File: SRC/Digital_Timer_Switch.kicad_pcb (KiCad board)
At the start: 2 copper layers, 82.5 x 76.2 mm, 65 parts, among them J101 AC_IN, J102 Conn_VIN, J103 AC_OUT, Q101 AO3401A, Q201 AO3401A, Q401 MMBT3904, SW301 SW_AUTO, SW302 SW_TIME, SW303 SW_DAY, SW304 SW_RST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

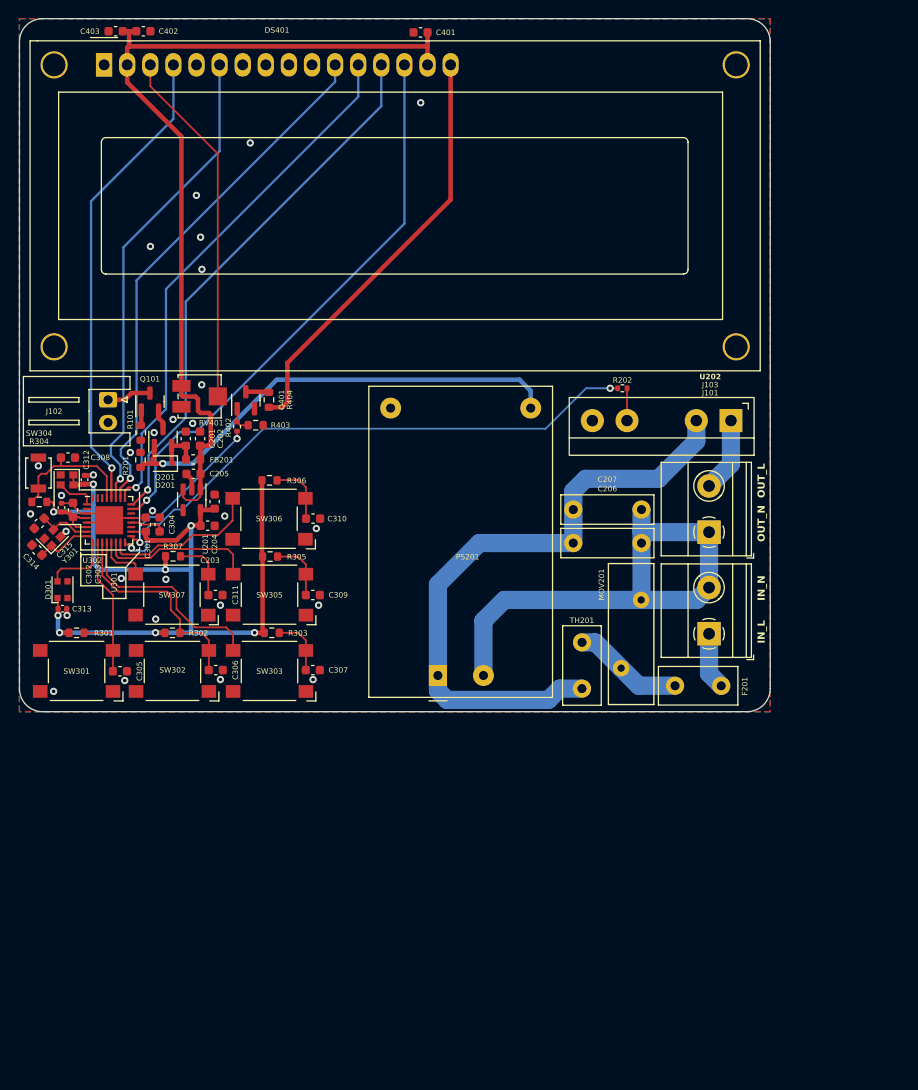
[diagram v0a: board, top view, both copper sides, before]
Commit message: Added debug testpoints.
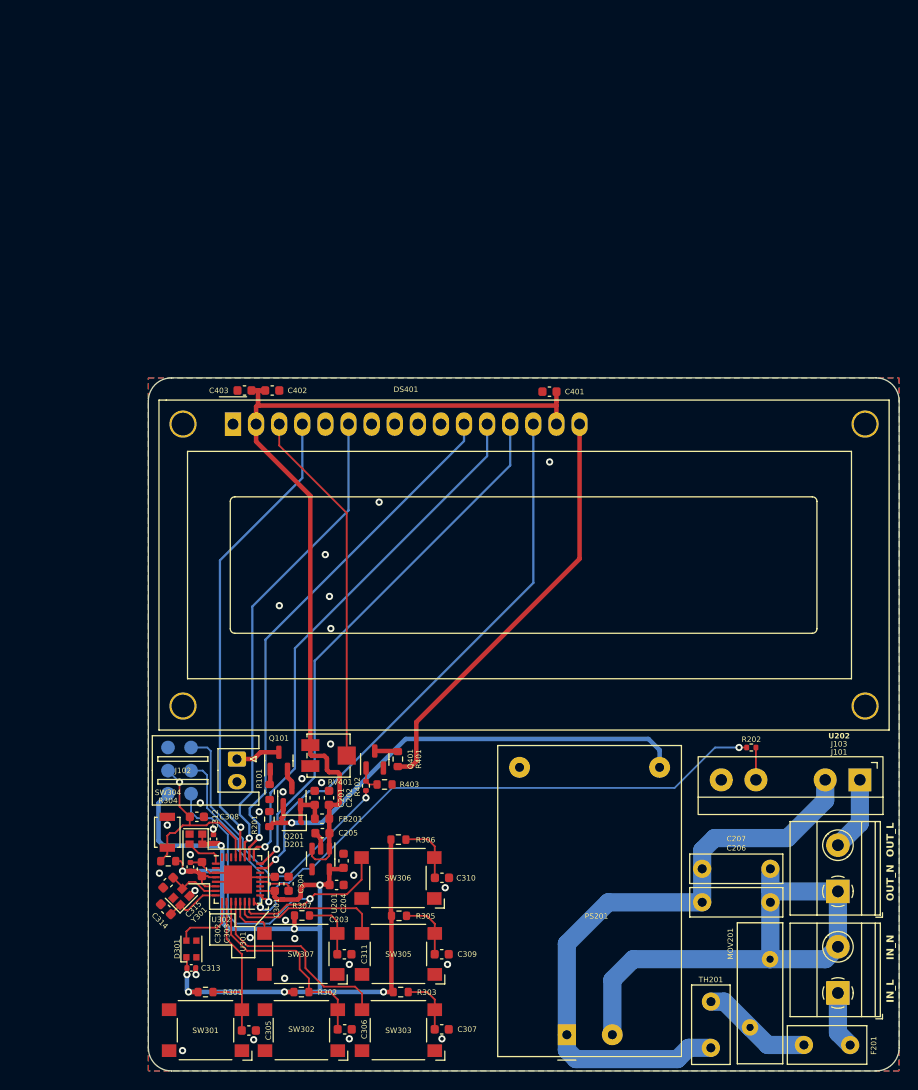
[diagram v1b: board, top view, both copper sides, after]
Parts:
- added TP301: TP_MOSI, TestPoint:TestPoint_Pad_D1.5mm, B.Cu at (107.8, 110.6)
- added TP302: TP_VCC, TestPoint:TestPoint_Pad_D1.5mm, B.Cu at (105.2, 110.6)
- added TP303: TP_MISO, TestPoint:TestPoint_Pad_D1.5mm, B.Cu at (107.8, 108.1)
- added TP304: TP_RST, TestPoint:TestPoint_Pad_D1.5mm, B.Cu at (105.2, 108.1)
- added TP305: TP_SCK, TestPoint:TestPoint_Pad_D1.5mm, B.Cu at (107.8, 105.5)
- added TP306: TP_GND, TestPoint:TestPoint_Pad_D1.5mm, B.Cu at (105.2, 105.5)
- moved MOV201 42.0 mm to (169.2, 136.3)
- moved R303 42.0 mm to (130.8, 132.4)
- moved C202 42.0 mm to (122.9, 111.1)
- moved C205 42.0 mm to (122.2, 115.0)
- moved C306 42.0 mm to (124.7, 136.5)
- moved C308 42.0 mm to (108.4, 113.2)
- moved C309 42.0 mm to (135.3, 128.3)
- moved C311 42.0 mm to (124.6, 128.3)
- moved C312 42.0 mm to (110.2, 115.6)
- moved C315 42.0 mm to (105.3, 120.4)
- moved C401 42.0 mm to (147.2, 66.4)
- moved D201 42.0 mm to (118.8, 113.8)
- moved FB201 42.0 mm to (122.2, 113.4)
- moved J103 42.0 mm to (178.9, 121.4)
- moved PS201 42.0 mm to (149.1, 137.1)
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- renumbered R404 to R401
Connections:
- net /Digital_Timer_Switch_Power/RELAY_EN renamed /MCU_ATMEGA328P-M/PB4
- net /MCU_ATMEGA328P-M/BTN_AUTO renamed /MCU_ATMEGA328P-M/PD6
- net /MCU_ATMEGA328P-M/BTN_DAY renamed /MCU_ATMEGA328P-M/PB0
- net /MCU_ATMEGA328P-M/BTN_HOUR renamed /MCU_ATMEGA328P-M/PB2
- net /MCU_ATMEGA328P-M/BTN_MIN renamed /MCU_ATMEGA328P-M/PB3
- net /MCU_ATMEGA328P-M/BTN_PROG renamed /MCU_ATMEGA328P-M/PB1
- net /MCU_ATMEGA328P-M/BTN_TIME renamed /MCU_ATMEGA328P-M/PD7
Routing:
- net /MCU_ATMEGA328P-M/PB3: track 24.5 -> 51.0 mm, vias 0 -> 1
- net /MCU_ATMEGA328P-M/PB5: track 18.5 -> 37.8 mm
- net /MCU_ATMEGA328P-M/PB4: track 63.2 -> 82.0 mm
- net +3V3: track 106.6 -> 119.6 mm
- net /MCU_ATMEGA328P-M/NRST: track 14.9 -> 21.0 mm, vias 0 -> 1
- net GND: track 17.5 -> 17.1 mm, vias 29 -> 31
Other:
- board text added: "+3V3"
- board text added: "GND"
- board text added: "MISO"
- board text added: "MOSI"
- board text added: "RST"
- board text added: "SCK"
